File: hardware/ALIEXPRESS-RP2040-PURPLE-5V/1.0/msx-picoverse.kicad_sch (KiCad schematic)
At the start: 10 parts, among them J1 Conn_01x04, U1 74LVC541, U2 RP2040-PURPLE

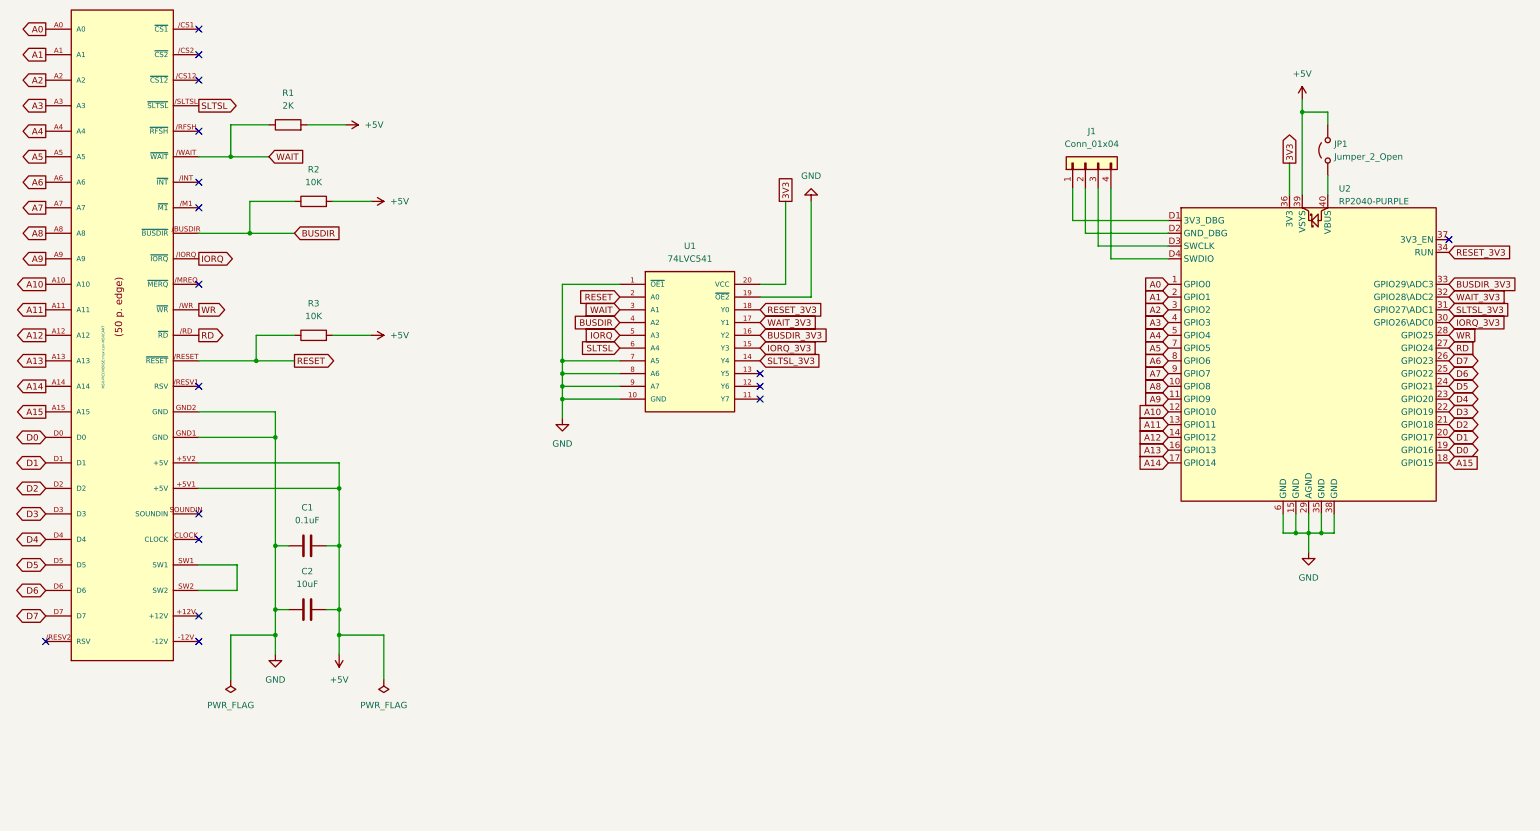
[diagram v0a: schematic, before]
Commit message: Schottky diode to prevent the pico powering the MSX
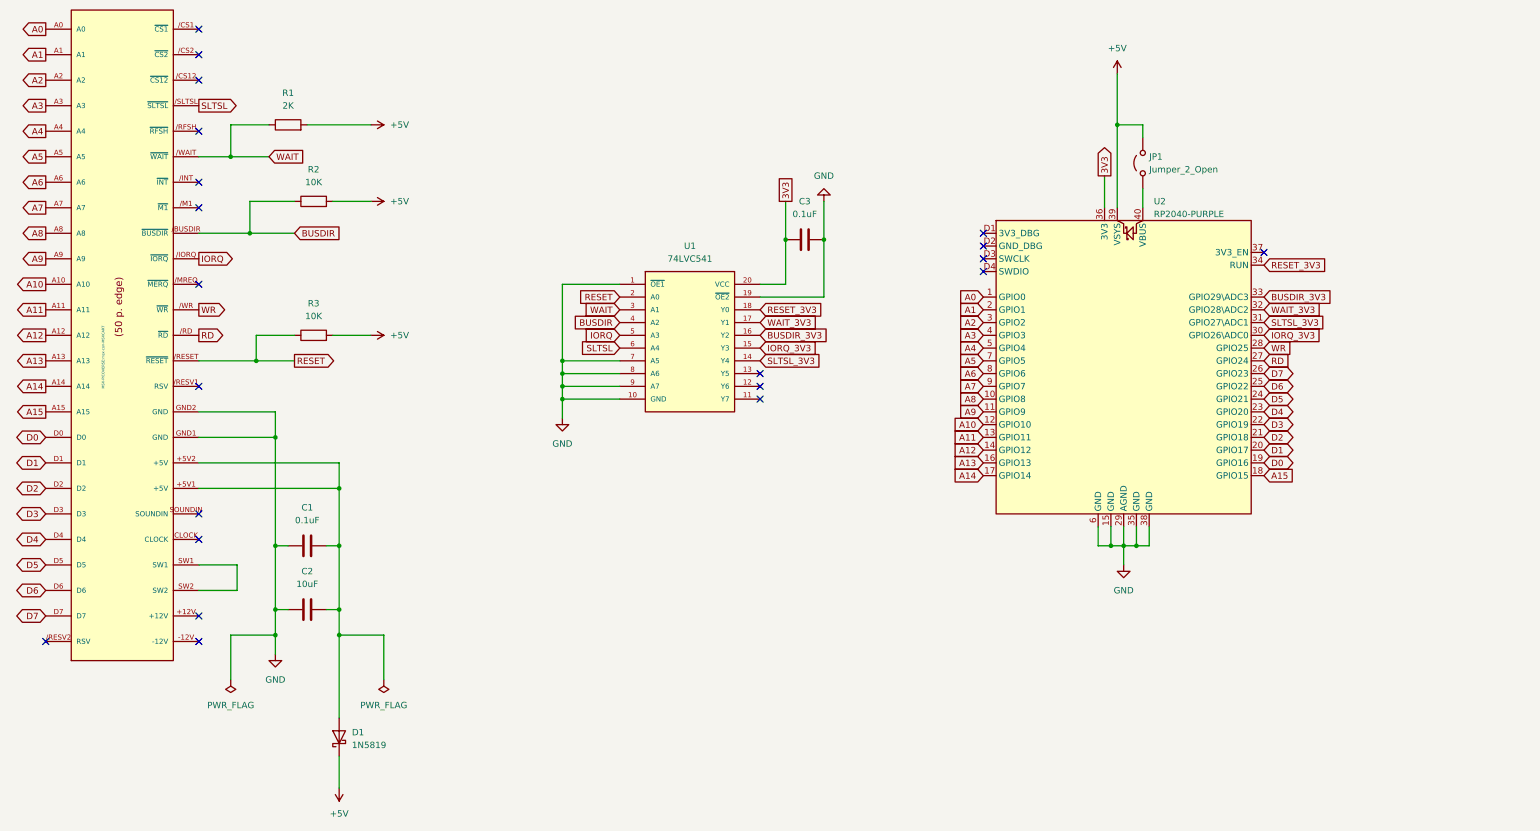
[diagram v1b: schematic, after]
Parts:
- removed J1: Conn_01x04, Connector_PinHeader_2.54mm:PinHeader_1x04_P2.54mm_Vertical, symbol Connector_Generic:Conn_01x04
- added C3: 0.1uF, Capacitor_SMD:C_0603_1608Metric_Pad1.08x0.95mm_HandSolder, symbol Device:C
- added D1: 1N5819, Diode_SMD:D_SOD-123, symbol Device:D_Schottky
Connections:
- net +5V: now also D1.1 (K); no longer C1.2, C2.2, EDG1.+5V1 (+5V), EDG1.+5V2 (+5V)
- net 3V3: now also C3.1
- net GND: now also C3.2
- new net: C1.2, C2.2, D1.2 (A), EDG1.+5V1 (+5V), EDG1.+5V2 (+5V)
- no-connect marks 17 -> 21
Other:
- moved on the sheet: JP1, U2
